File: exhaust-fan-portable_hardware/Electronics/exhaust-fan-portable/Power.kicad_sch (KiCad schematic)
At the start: 7 parts, among them Q3 NMOS, U4 LM78M05_TO252, U5 AMS1117-3.3, U6 AMS1117-3.3

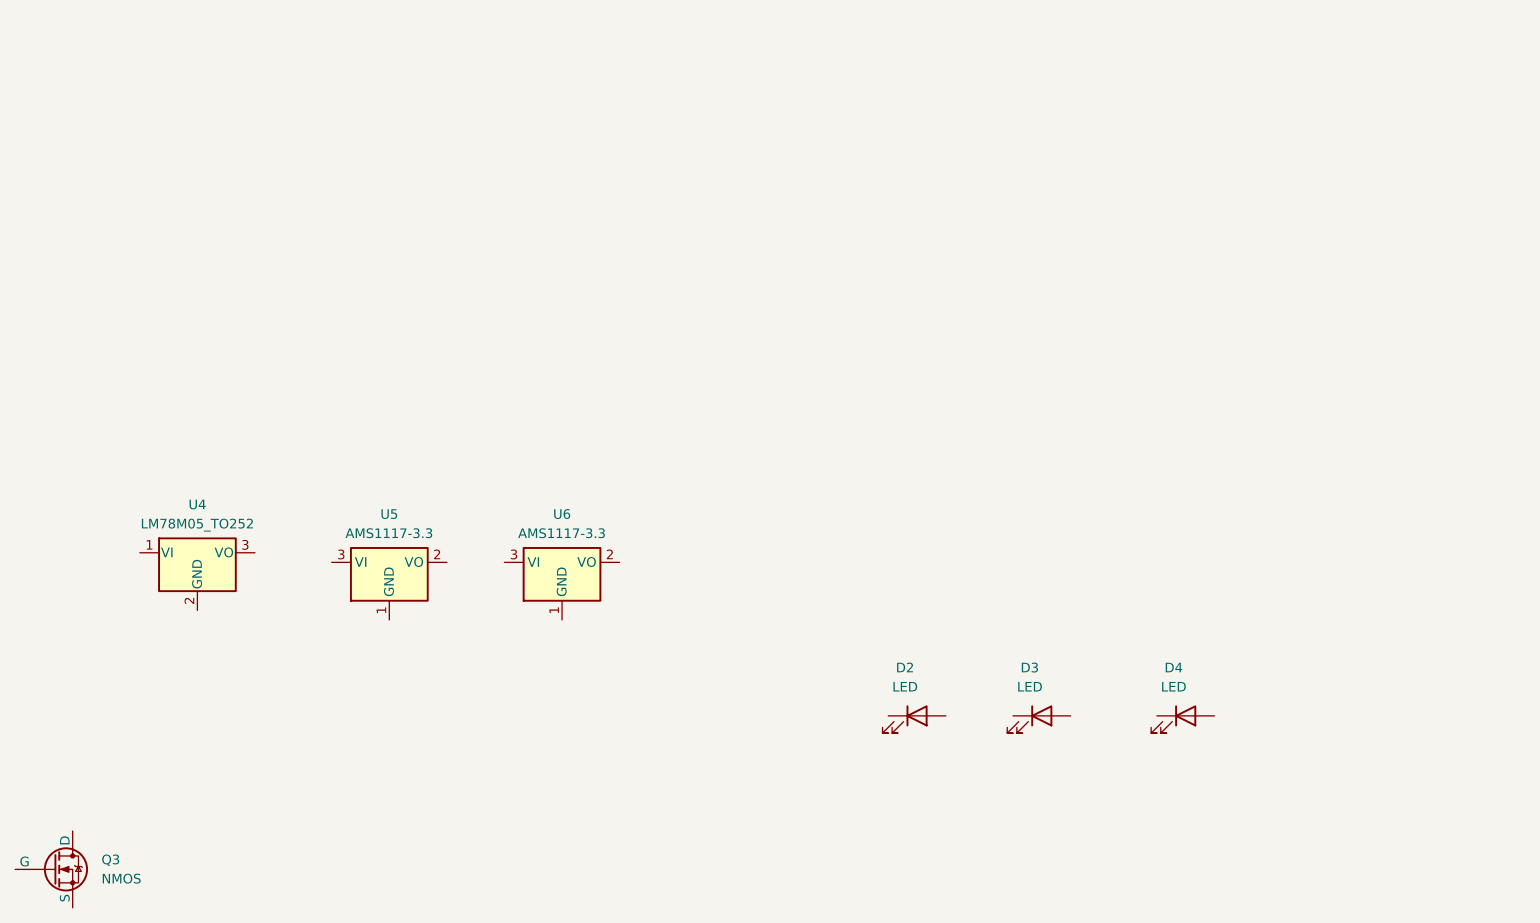
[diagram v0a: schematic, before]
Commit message: layed out rough schematic and added sensor comparison
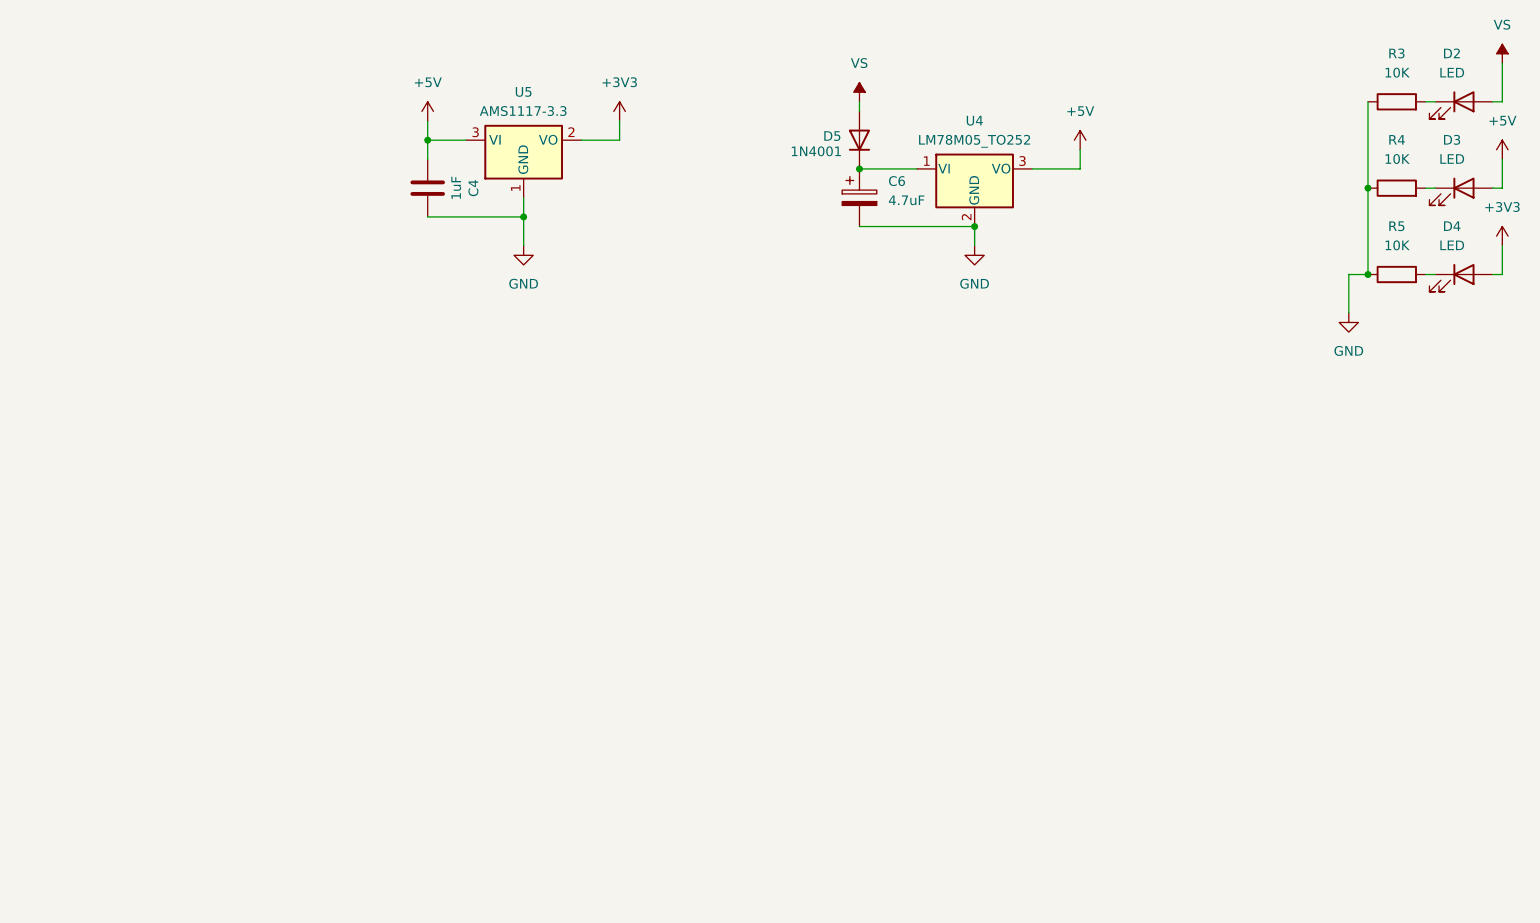
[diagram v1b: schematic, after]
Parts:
- removed Q3: NMOS, symbol Simulation_SPICE:NMOS
- removed U6: AMS1117-3.3, Package_TO_SOT_SMD:SOT-223-3_TabPin2, symbol Regulator_Linear:AMS1117-3.3
- added C4: 1uF, symbol Device:C
- added C6: 4.7uF, symbol Device:C_Polarized
- added D5: 1N4001, Diode_THT:D_DO-41_SOD81_P10.16mm_Horizontal, symbol Diode:1N4001
- added R3, R4, R5: 10K, symbol Device:R
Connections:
- net at D4.1 (K): now also R5.2
- net +3V3: now reaches D4.2 (A)
- net +3V3: now also U5.2 (VO)
- net GND: now reaches U5.1 (GND)
- net GND: now also U4.2 (GND), C4.1, C6.2, R3.1, R4.1, R5.1
- net +5V: now reaches U5.3 (VI)
- net +5V: now also D3.2 (A), U4.3 (VO), C4.2
- net at D2.1 (K): now also R3.2
- net VS: now reaches D2.2 (A)
- net VS: now also D5.2 (A)
- net at U4.1 (VI): now also C6.1, D5.1 (K)
- net at D3.1 (K): now also R4.2
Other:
- moved on the sheet: D2, D3, D4, U4, U5

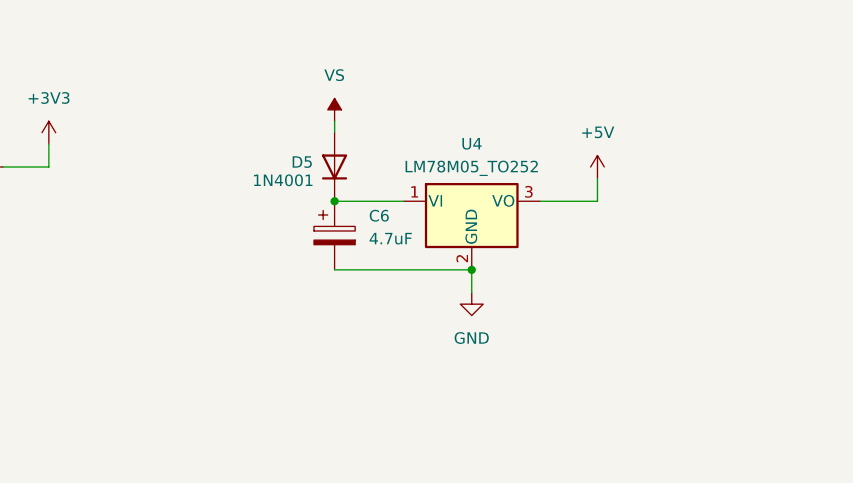
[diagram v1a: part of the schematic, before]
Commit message: fixed case design
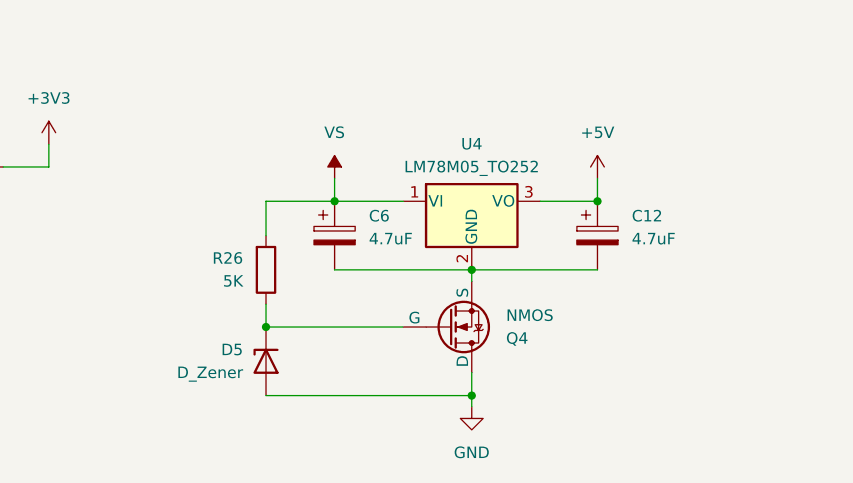
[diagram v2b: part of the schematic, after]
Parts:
- removed D5: 1N4001, Diode_THT:D_DO-41_SOD81_P10.16mm_Horizontal, symbol Diode:1N4001
- added C12: 4.7uF, Capacitor_SMD:C_1206_3216Metric_Pad1.33x1.80mm_HandSolder, symbol Device:C_Polarized
- added D5: D_Zener, Diode_SMD:D_1206_3216Metric_Pad1.42x1.75mm_HandSolder, symbol Device:D_Zener
- added Q4: NMOS, Package_TO_SOT_SMD:TO-263-2, symbol Simulation_SPICE:NMOS
- added R26: 5K, Resistor_SMD:R_0603_1608Metric_Pad0.98x0.95mm_HandSolder, symbol Device:R
- C4: footprint (none) -> Capacitor_SMD:C_0805_2012Metric_Pad1.18x1.45mm_HandSolder
- C6: footprint (none) -> Capacitor_SMD:C_1206_3216Metric_Pad1.33x1.80mm_HandSolder
- D2, D3, D4: footprint (none) -> LED_SMD:LED_0603_1608Metric_Pad1.05x0.95mm_HandSolder
- R3, R4, R5: footprint (none) -> Resistor_SMD:R_0603_1608Metric_Pad0.98x0.95mm_HandSolder
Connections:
- net +5V: now also C12.1
- net GND: now also D5.2 (A), Q4.1 (D); no longer C6.2, U4.2 (GND)
- net VS: now also C6.1, U4.1 (VI), R26.2
- new net: D5.1 (K), Q4.2 (G), R26.1
- new net: C12.2, C6.2, Q4.3 (S), U4.2 (GND)

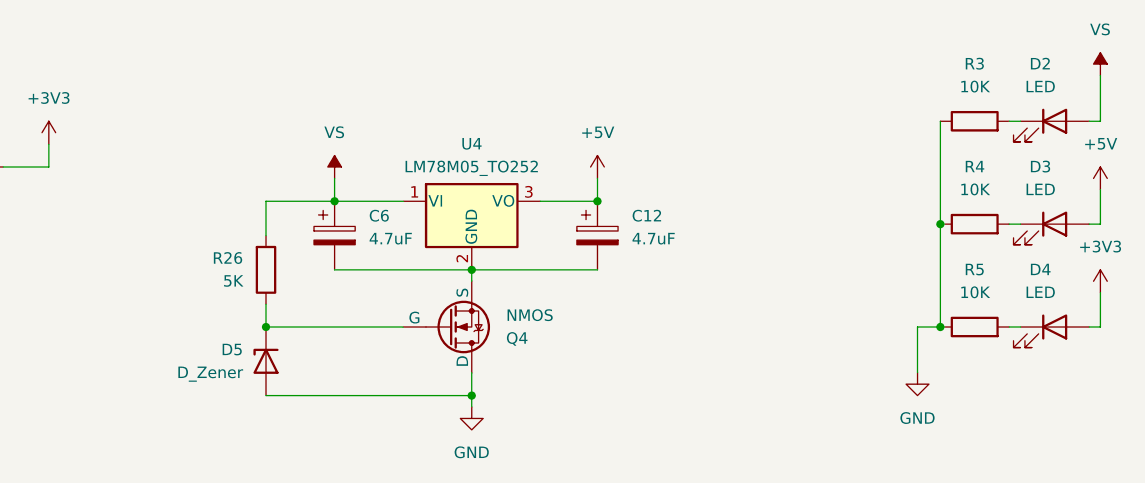
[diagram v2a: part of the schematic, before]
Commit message: updated mechanical information
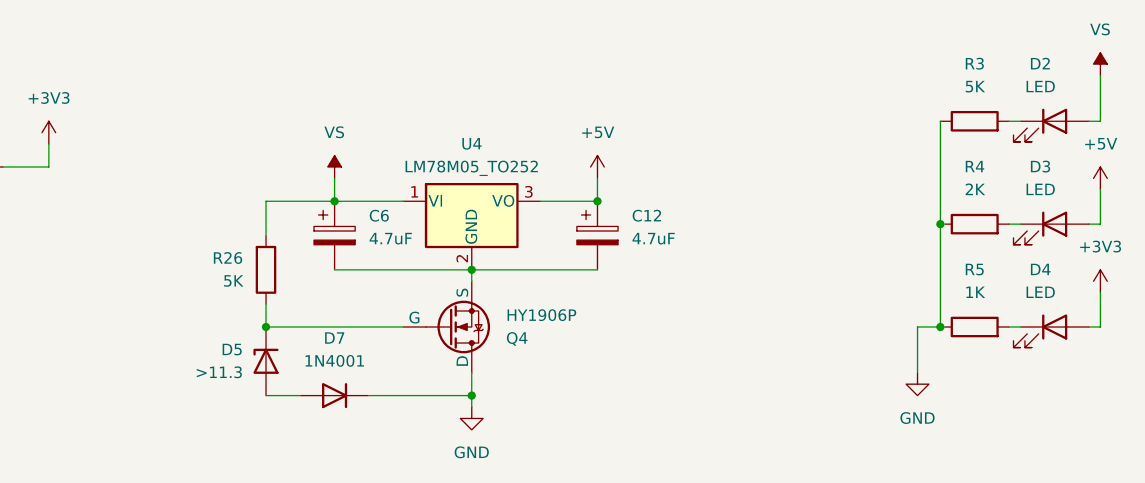
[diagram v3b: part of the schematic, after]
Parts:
- added D7: 1N4001, Diode_SMD:D_SOD-323_HandSoldering, symbol Diode:1N4001
- D5: value D_Zener -> >11.3
- Q4: value NMOS -> HY1906P
- R3: value 10K -> 5K
- R4: value 10K -> 2K
- R5: value 10K -> 1K
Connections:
- net GND: now also D7.1 (K); no longer D5.2 (A)
- new net: D5.2 (A), D7.2 (A)
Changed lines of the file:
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@@
+	)
+	(junction
+		(at 195.58 64.77)
+		(diameter 0)
+		(color 0 0 0 0)
 	)
 	(junction
@@
 	)
 	(junction
-		(at 195.58 64.77)
-		(diameter 0)
-		(color 0 0 0 0)
-	)
-	(junction
 		(at 195.58 50.8)
 		(diameter 0)
@@
 	(wire
 		(pts
-			(xy 172.72 64.77) (xy 195.58 64.77)
-		)
-		(stroke
-			(width 0)
-			(type default)
-		)
-	)
-	(wire
-		(pts
 			(xy 265.43 41.91) (xy 265.43 45.72)
 		)
@@
 	(wire
 		(pts
-			(xy 195.58 66.04) (xy 195.58 64.77)
-		)
-		(stroke
-			(width 0)
-			(type default)
-		)
-	)
-	(wire
-		(pts
 			(xy 255.27 57.15) (xy 256.54 57.15)
 		)
@@
 	(wire
 		(pts
-			(xy 195.58 64.77) (xy 195.58 62.23)
+			(xy 184.15 64.77) (xy 195.58 64.77)
+		)
+		(stroke
+			(width 0)
+			(type default)
+		)
+	)
+	(wire
+		(pts
+			(xy 172.72 64.77) (xy 176.53 64.77)
+		)
+		(stroke
+			(width 0)
+			(type default)
+		)
+	)
+	(wire
+		(pts
+			(xy 195.58 62.23) (xy 195.58 64.77)
 		)
 		(stroke
@@
 		(pts
 			(xy 123.19 49.53) (xy 135.89 49.53)
+		)
+		(stroke
+			(width 0)
+			(type default)
+		)
+	)
+	(wire
+		(pts
+			(xy 195.58 64.77) (xy 195.58 66.04)
 		)
 		(stroke
@@
 			)
 		)
-		(property "Value" "D_Zener"
+		(property "Value" ">11.3"
 			(at 170.18 62.2299 90)
 			(effects
@@
 			)
 		)
-		(property "Value" "10K"
+		(property "Value" "2K"
 			(at 251.46 41.91 90)
 			(effects
@@
 			)
 		)
-		(property "Value" "NMOS"
+		(property "Value" "HY1906P"
 			(at 199.39 55.8801 0)
 			(effects
@@
 			)
 		)
-		(property "Value" "10K"
+		(property "Value" "1K"
 			(at 251.46 53.34 90)
 			(effects
@@
 	)
 	(symbol
+		(lib_id "Diode:1N4001")
+		(at 180.34 64.77 180)
+		(unit 1)
+		(exclude_from_sim no)
+		(in_bom yes)
+		(on_board yes)
+		(dnp no)
+		(fields_autoplaced yes)
+		(property "Reference" "D7"
+			(at 180.34 58.42 0)
+			(effects
+				(font
+					(size 1.27 1.27)
+				)
+			)
+		)
+		(property "Value" "1N4001"
+			(at 180.34 60.96 0)
+			(effects
+				(font
+					(size 1.27 1.27)
+				)
+			)
+		)
+		(property "Footprint" "Diode_SMD:D_SOD-323_HandSoldering"
+			(at 180.34 64.77 0)
+			(effects
+				(font
+					(size 1.27 1.27)
+				)
+				(hide yes)
+			)
+		)
+		(property "Datasheet" "http://www.vishay.com/docs/88503/1n4001.pdf"
+			(at 180.34 64.77 0)
+			(effects
+				(font
+					(size 1.27 1.27)
+				)
+				(hide yes)
+			)
+		)
+		(property "Description" "50V 1A General Purpose Rectifier Diode, DO-41"
+			(at 180.34 64.77 0)
+			(effects
+				(font
+					(size 1.27 1.27)
+				)
+				(hide yes)
+			)
+		)
+		(property "Sim.Device" "D"
+			(at 180.34 64.77 0)
+			(effects
+				(font
+					(size 1.27 1.27)
+				)
+				(hide yes)
+			)
+		)
+		(property "Sim.Pins" "1=K 2=A"
+			(at 180.34 64.77 0)
+			(effects
+				(font
+					(size 1.27 1.27)
+				)
+				(hide yes)
+			)
+		)
+		(pin "2"
+		)
+		(pin "1"
+		)
+		(instances
+			(project ""
+				(path "/055e7171-e611-4dda-a539-d65a04d953db/e6f54a4e-e20c-4741-b880-e5ee206a27c1"
+					(reference "D7")
+					(unit 1)
+				)
+			)
+		)
+	)
+	(symbol
 		(lib_id "power:GND")
 		(at 195.58 66.04 0)
@@
 			)
 		)
-		(property "Value" "10K"
+		(property "Value" "5K"
 			(at 251.46 30.48 90)
 			(effects
